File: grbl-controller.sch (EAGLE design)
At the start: 5 parts, among them IC1 MEGA8-P, IC2 FT232RL, IC3 ADUM1250, X1 PN61729-S

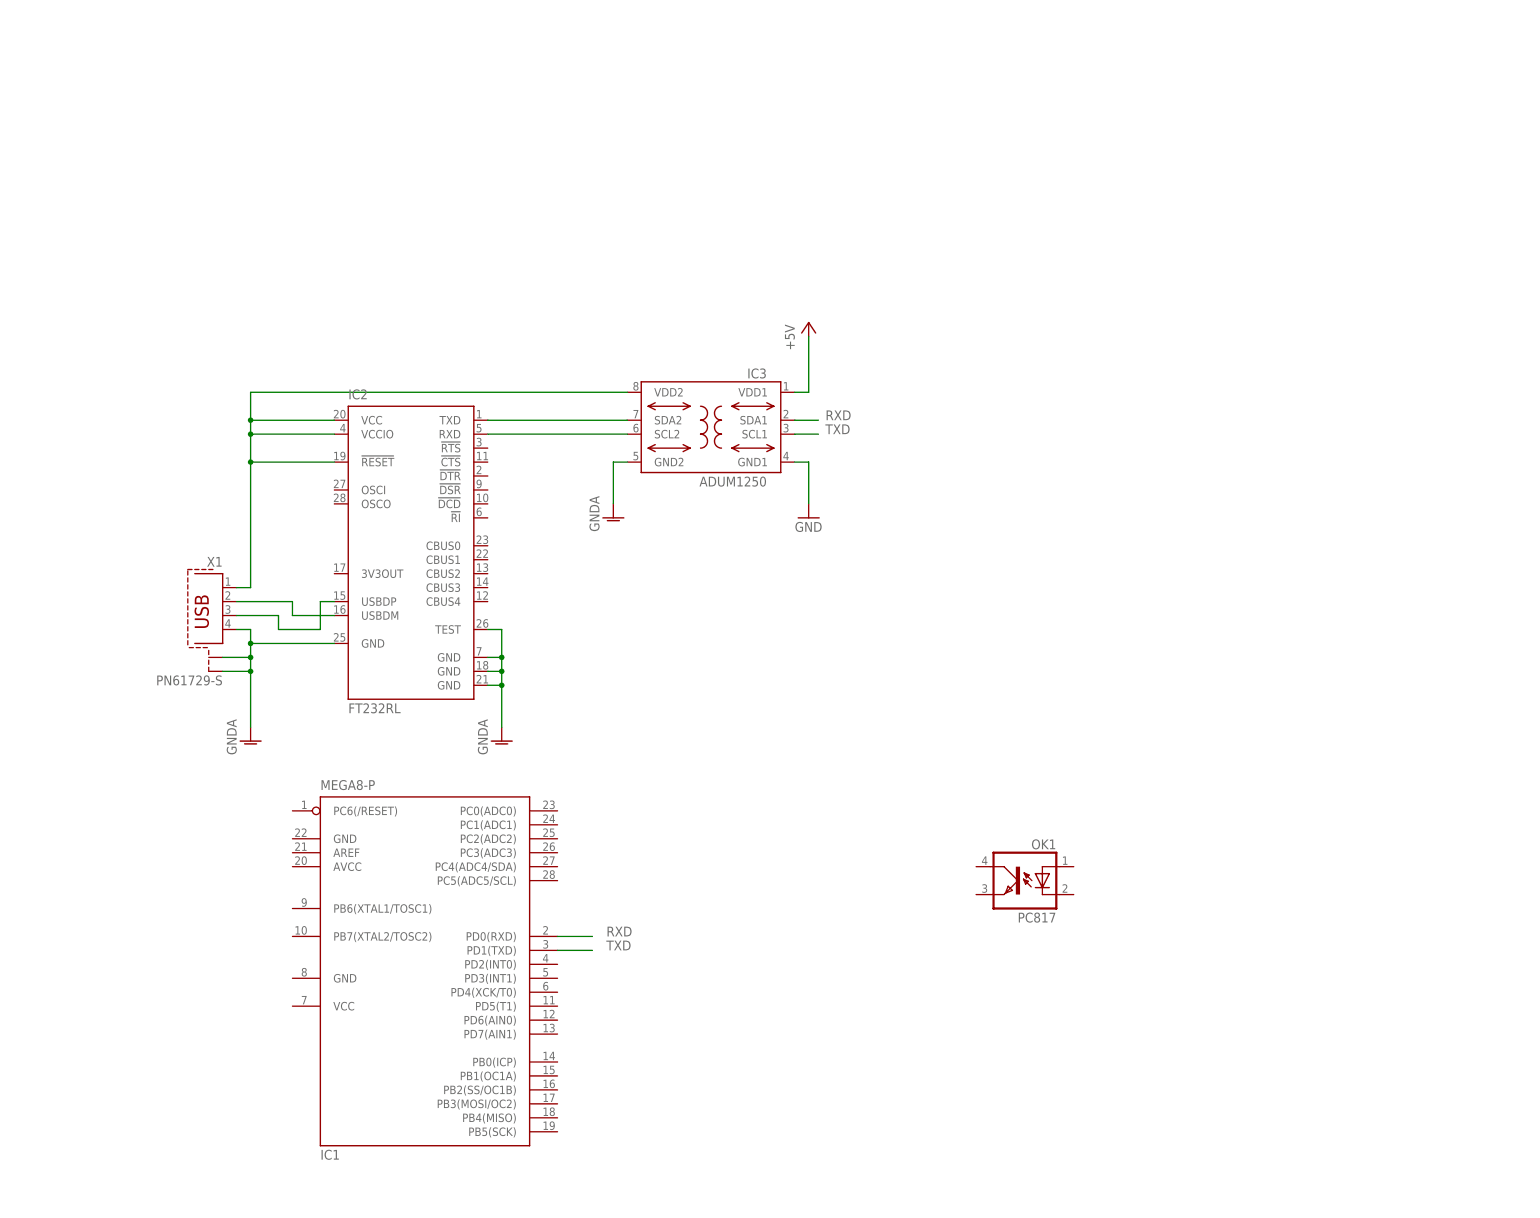
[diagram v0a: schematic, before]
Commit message: add xyz-limits
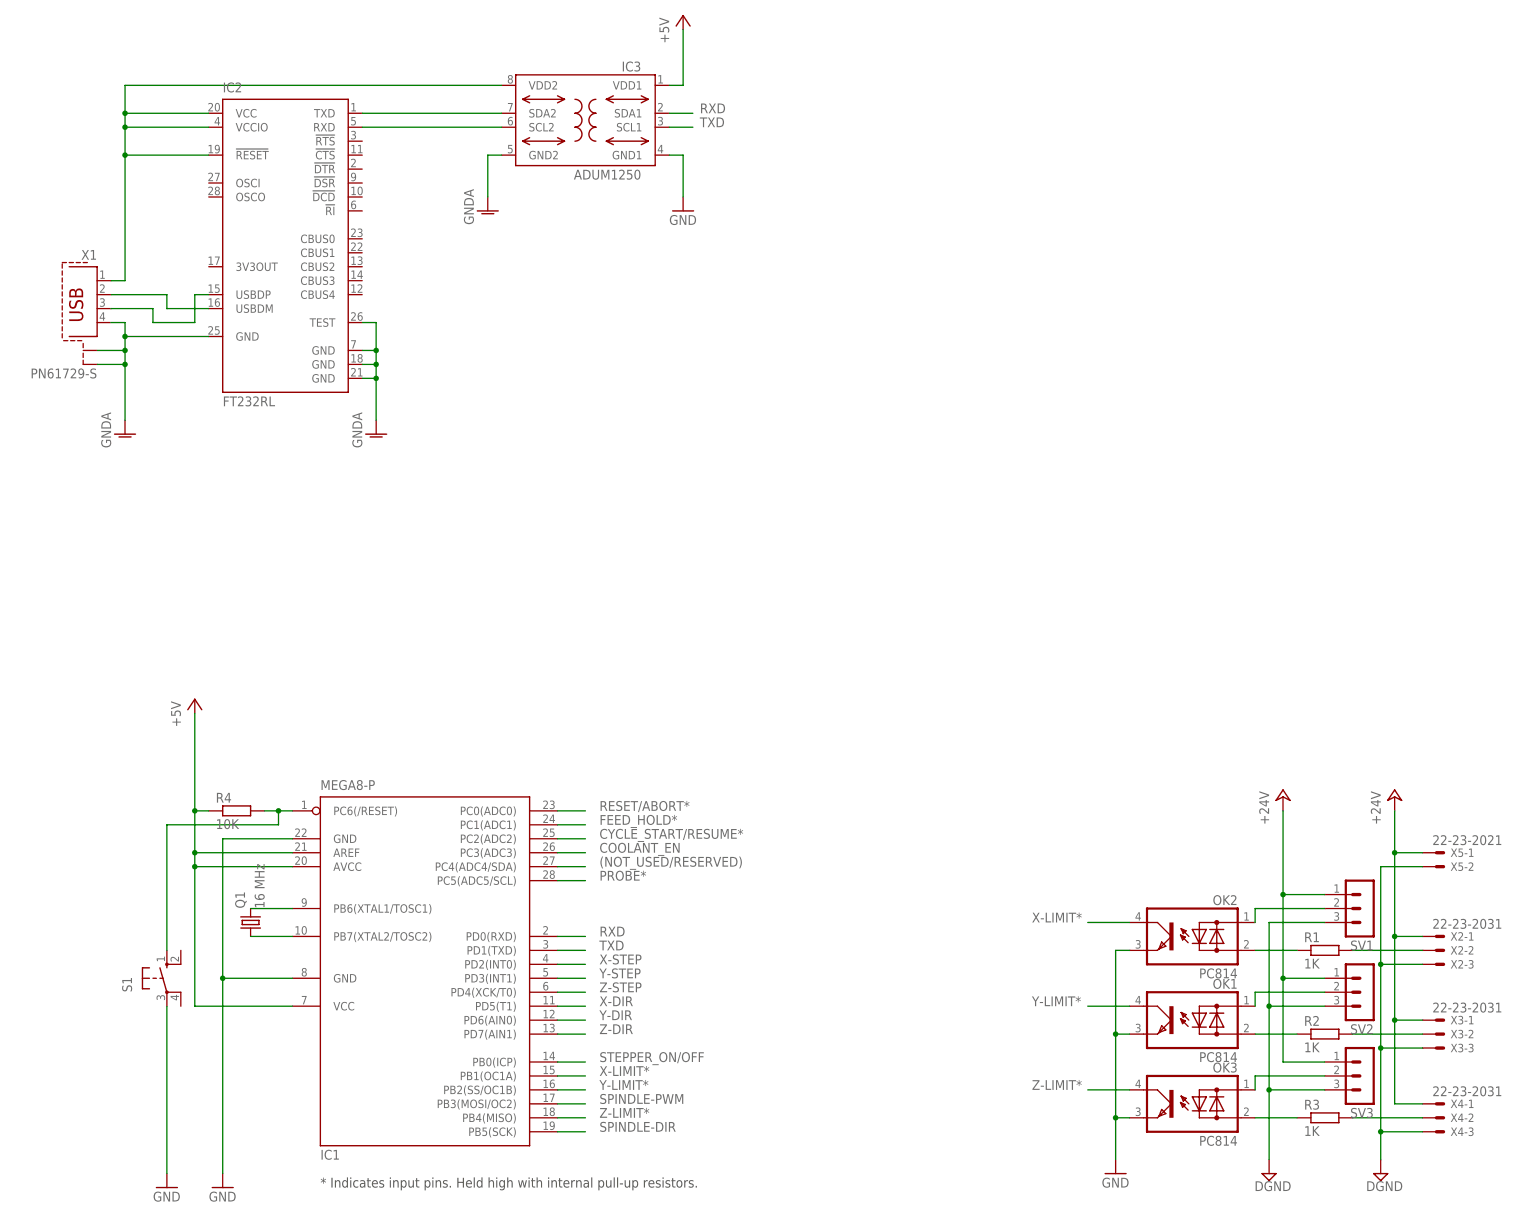
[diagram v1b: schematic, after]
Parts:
- added OK2, OK3: PC814, optocoupler:PC814
- added Q1: 16 MHz, crystal:CRYSTALHC49S
- added R1, R2, R3: 1K, resistor:R-EU_M0805
- added R4: 10K, resistor:R-EU_M0805
- added S1: (no value), switch-omron:10-XX
- added SV1, SV2, SV3: (no value), con-lstb:MA03-1
- added X2, X3, X4: 22-23-2031, con-molex:22-23-2031
- added X5: 22-23-2021, con-molex:22-23-2021
- OK1: value PC817 -> PC814; device optocoupler:PC817 -> optocoupler:PC814
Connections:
- new net (NOT_USED/RESERVED): IC1.PC4(ADC4/SDA)
- new net +24V: SV1.1, SV2.1, SV3.1, X2-1.S, X3-1.S, X4-1.S, X5-1.S
- new net +5V: IC1.AREF, IC1.AVCC, IC1.VCC@1, R4.1
- new net COOLANT_EN: IC1.PC3(ADC3)
- new net CYCLE_START/RESUME*: IC1.PC2(ADC2)
- new net DGND: SV1.3, SV2.3, SV3.3, X2-3.S, X3-3.S, X4-3.S, X5-2.S
- new net FEED_HOLD*: IC1.PC1(ADC1)
- new net N$10: OK3.AC1, SV3.2
- new net N$11: OK1.AC1, SV2.2
- new net N$12: OK2.AC1, SV1.2
- new net N$13: R1.2, X2-2.S
- new net N$14: OK3.AC2, R3.1
- new net N$15: OK1.AC2, R2.1
- new net N$16: IC1.PC6(/RESET), R4.2, S1.S
- new net N$5: OK2.AC2, R1.1
- new net N$6: IC1.PB6(XTAL1/TOSC1), Q1.2
- new net N$7: IC1.PB7(XTAL2/TOSC2), Q1.1
- new net N$8: R2.2, X3-2.S
- new net N$9: R3.2, X4-2.S
- new net PROBE*: IC1.PC5(ADC5/SCL)
- new net RESET/ABORT*: IC1.PC0(ADC0)
- new net SPINDLE-DIR: IC1.PB5(SCK)
- new net SPINDLE-PWM: IC1.PB3(MOSI/OC2)
- new net STEPPER_ON/OFF: IC1.PB0(ICP)
- new net X-DIR: IC1.PD5(T1)
- new net X-LIMIT*: IC1.PB1(OC1A), OK2.C
- new net X-STEP: IC1.PD2(INT0)
- new net Y-DIR: IC1.PD6(AIN0)
- new net Y-LIMIT*: IC1.PB2(SS/OC1B), OK1.C
- new net Y-STEP: IC1.PD3(INT1)
- new net Z-DIR: IC1.PD7(AIN1)
- new net Z-LIMIT*: IC1.PB4(MISO), OK3.C
- new net Z-STEP: IC1.PD4(XCK/T0)
- net GND: now also IC1.GND, IC1.GND@1, OK1.E, OK2.E, OK3.E, S1.P
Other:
- note added: "* Indicates input pins. Held high with internal pull-up resistors."
- moved on the sheet: IC2, IC3, X1
